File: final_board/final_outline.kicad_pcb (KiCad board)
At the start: 2 copper layers, 99.5 x 75 mm, 46 parts, among them P001 CANCONNECTOR, P002 AUXCONNECTOR, P100 ISP, P101 DEBUG_LED, U402 MCP2551-I/SN, U403 LPC11C14, U501 MCP1755-33, U502 MCP1755-5, U503 Zsr1000gta, U601 LM358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

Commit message: Resistor values changed from 1k to 100k
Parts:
- R601, R602: value 1k -> 100k
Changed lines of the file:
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@@
-(kicad_pcb (version 4) (host pcbnew 4.0.1-stable)
+(kicad_pcb (version 4) (host pcbnew 4.0.0-stable)
   (general
     (links 117)
     (no_connects 0)
-    (area 98.806 49.875 215 135.483792)
+    (area 102.424999 52.924999 202.075001 128.075001)
     (thickness 1.6)
     (drawings 6)
@@
       (effects (font (size 1 1) (thickness 0.15)))
     )
-    (fp_text value 1k (at -2.794 0 180) (layer F.Fab)
+    (fp_text value 100k (at -2.794 0.508 180) (layer F.Fab)
       (effects (font (size 1 1) (thickness 0.15)))
     )
@@
       (effects (font (size 1 1) (thickness 0.15)))
     )
-    (fp_text value 1k (at 2.794 0 360) (layer F.Fab)
-      (effects (font (size 1 1) (thickness 0.15)))
-    )
+    (fp_text value 100k (at 2.921 0.381 360) (layer F.Fab)
+      (effects (font (size 1 1) (thickness 0.15)))
+    )

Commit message: Added ground via
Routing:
- net GND: track 43.2 -> 45.7 mm, vias 11 -> 12
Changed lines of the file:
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@@
-(kicad_pcb (version 4) (host pcbnew 4.0.0-stable)
+(kicad_pcb (version 4) (host pcbnew 4.0.4+e1-6308~48~ubuntu16.04.1-stable)
   (general
     (links 117)
     (no_connects 0)
-    (area 102.424999 52.924999 202.075001 128.075001)
+    (area 98.806 50.025 214.85 135.483792)
     (thickness 1.6)
     (drawings 6)
-    (tracks 425)
+    (tracks 428)
     (zones 0)
     (modules 46)
@@
   (segment (start 141.97 70.15) (end 141.97 70.3) (width 0.25) (layer F.Cu) (net 24))
   (segment (start 139 67.18) (end 141.97 70.15) (width 0.25) (layer F.Cu) (net 24))
+  (segment (start 124.65 92.8) (end 124.65 93.662) (width 0.5) (layer F.Cu) (net 25) (status 400000))
+  (via (at 125.476 94.996) (size 0.8) (drill 0.4) (layers F.Cu B.Cu) (net 25))
+  (segment (start 124.65 93.662) (end 125.476 94.996) (width 0.5) (layer F.Cu) (net 25))
   (segment (start 146.497 93.345) (end 146.497 95.303) (width 0.5) (layer F.Cu) (net 25))
   (via (at 145.2 96.6) (size 0.8) (drill 0.4) (layers F.Cu B.Cu) (net 25))

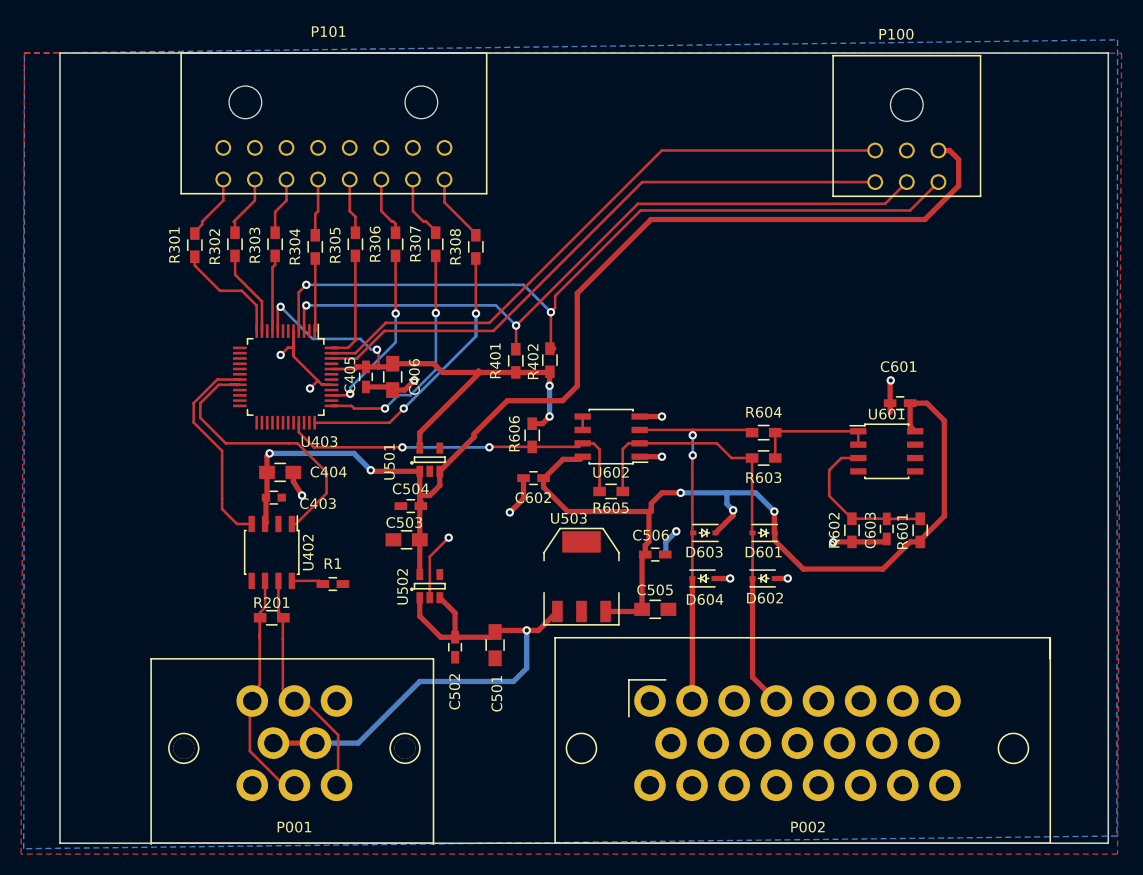
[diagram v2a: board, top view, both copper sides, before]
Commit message: Updated PCB by replacing old parts, fixing voltage regulator, adding test points, and general improvements
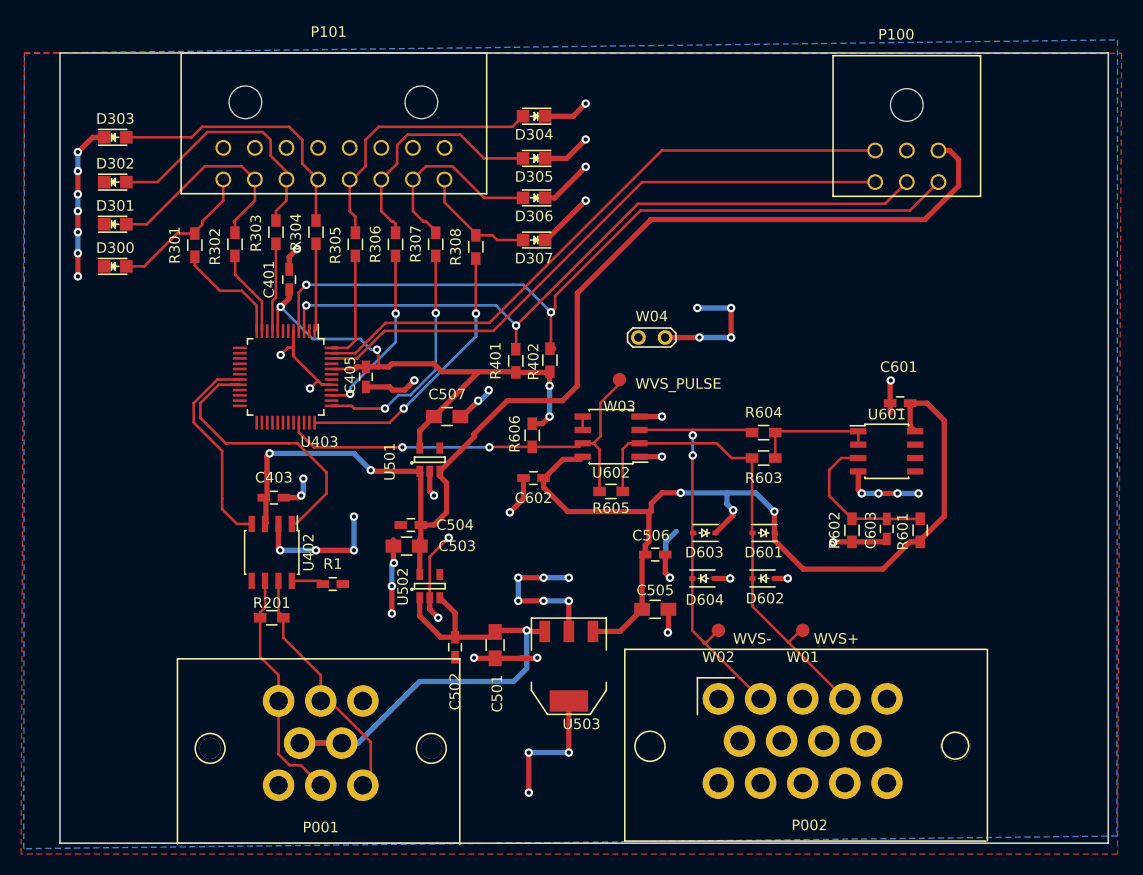
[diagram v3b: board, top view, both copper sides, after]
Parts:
- removed C404, C406: 10uF, Capacitors_SMD:C_0805_HandSoldering
- added C401: 0.1uF, Capacitors_SMD:C_0603_HandSoldering, F.Cu at (124.2, 74.5)
- added C507: 10μ, Capacitors_SMD:C_0805_HandSoldering, F.Cu at (139.2, 87.5)
- added D300: LED, LEDs:LED_0805, F.Cu at (107.8, 73.2)
- added D301: LED, LEDs:LED_0805, F.Cu at (107.8, 69.2)
- added D302: LED, LEDs:LED_0805, F.Cu at (107.8, 65.2)
- added D303: LED, LEDs:LED_0805, F.Cu at (107.8, 61.0)
- added D304: LED, LEDs:LED_0805, F.Cu at (147.5, 59.0)
- added D305: LED, LEDs:LED_0805, F.Cu at (147.5, 63.0)
- added D306: LED, LEDs:LED_0805, F.Cu at (147.5, 66.8)
- added D307: LED, LEDs:LED_0805, F.Cu at (147.5, 70.8)
- added W01: TEST_1P, MITEVT_TP:smd_test_pad, F.Cu at (173.0, 107.8)
- added W02: TEST_1P, MITEVT_TP:smd_test_pad, F.Cu at (165.0, 107.8)
- added W03: TEST_1P, MITEVT_TP:smd_test_pad, F.Cu at (155.6, 84.0)
- added W04: TEST, Measurement_Points:Test_Point_2Pads, F.Cu at (157.4, 80.0)
- C403: footprint Capacitors_SMD:C_0603 -> Capacitors_SMD:C_0603_HandSoldering
- P002: value AUXCONNECTOR -> CONN_01X14; footprint MITEVT_AUTOMOTIVECON:776087-1 -> MITEVT_AUTOMOTIVECON:776267-1
- P100: footprint Connectors_Molex:Connector_Microfit3_Header_02x03_Angled_43045-060x -> Connectors_Molex:Molex_Microfit3_Header_02x03_Angled_43045-060x
- P101: footprint Connectors_Molex:Connector_Microfit3_Header_02x08_Angled_43045-160x -> Connectors_Molex:Molex_Microfit3_Header_02x08_Angled_43045-160x
- moved U503 8.58 mm to (150.8, 111.2), turned to 180 degrees
- moved P002 6.51 mm to (165.0, 114.3)
- moved P001 2.50 mm to (123.2, 122.5)
- moved C504 1.80 mm to (135.8, 97.8)
- moved R304 1.40 mm to (126.8, 70.0)
- moved R303 1.15 mm to (123.0, 70.0)
- moved C503 0.60 mm to (135.4, 99.8)
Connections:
- net Net-(P101-Pad10) renamed /FRONT_PANEL/LED1_O
- net Net-(P101-Pad11) renamed /FRONT_PANEL/LED2_O
- net Net-(P101-Pad12) renamed /FRONT_PANEL/LED3_O
- net Net-(P101-Pad13) renamed /FRONT_PANEL/LED4_O
- net Net-(P101-Pad14) renamed /FRONT_PANEL/LED5_O
- net Net-(P101-Pad15) renamed /FRONT_PANEL/LED6_O
- net Net-(P101-Pad16) renamed /FRONT_PANEL/LED7_O
- net Net-(P101-Pad9) renamed /FRONT_PANEL/LED0_O
- P002 pad 15: Net-(P002-Pad15) -> (no net)
- P002 pad 16: Net-(P002-Pad16) -> (no net)
- U503 pad 1: +12V -> VCC
- U503 pad 3: VCC -> +12V
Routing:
- net GND: track 45.7 -> 169.9 mm, vias 12 -> 57
- net /FRONT_PANEL/LED3_O: track 5.41 -> 26.0 mm
- net /FRONT_PANEL/LED4_O: track 5.27 -> 25.7 mm
- net /FRONT_PANEL/LED2_O: track 5.50 -> 24.7 mm
- net /FRONT_PANEL/LED5_O: track 5.70 -> 22.9 mm
- net /FRONT_PANEL/LED1_O: track 5.92 -> 20.9 mm
- net /FRONT_PANEL/LED6_O: track 6.10 -> 18.3 mm
- net /FRONT_PANEL/LED0_O: track 6.25 -> 14.0 mm
- net /Micro_Controller/WVS_PULSE: track 34.4 -> 41.5 mm
- net /FRONT_PANEL/LED7_O: track 6.53 -> 11.2 mm
- net /BACK_PANEL/WVS-: track 36.6 -> 41.1 mm
- net /BACK_PANEL/WVS+: track 41.1 -> 45.5 mm
- net +5V: track 106.1 -> 110.0 mm
- net VCC: track 86.1 -> 88.4 mm
- net +12V: track 51.7 -> 49.8 mm
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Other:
- net class Default: clearance 0.2 -> 0.15
- net class POWER: clearance 0.2 -> 0.15
- rule trace_clearance: 0.2 -> 0.15
- board text added: "WVS+"
- board text added: "WVS-"
- board text added: "WVS_PULSE"
